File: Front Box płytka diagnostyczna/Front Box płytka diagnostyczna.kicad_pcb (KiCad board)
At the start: 2 copper layers, 54 x 27.7 mm, 7 parts, among them J1 hdmi wurth, J5 CAN

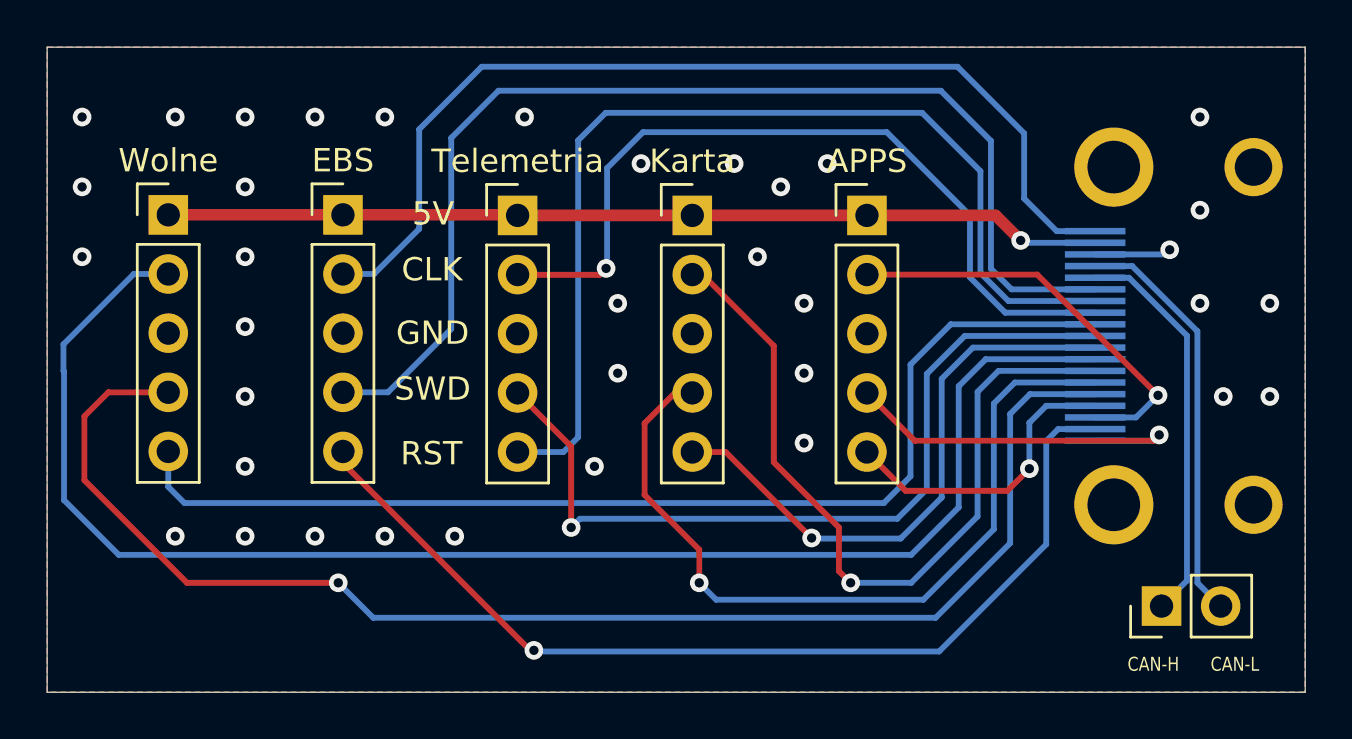
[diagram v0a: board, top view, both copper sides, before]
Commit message: PCB prepared for gerber generation
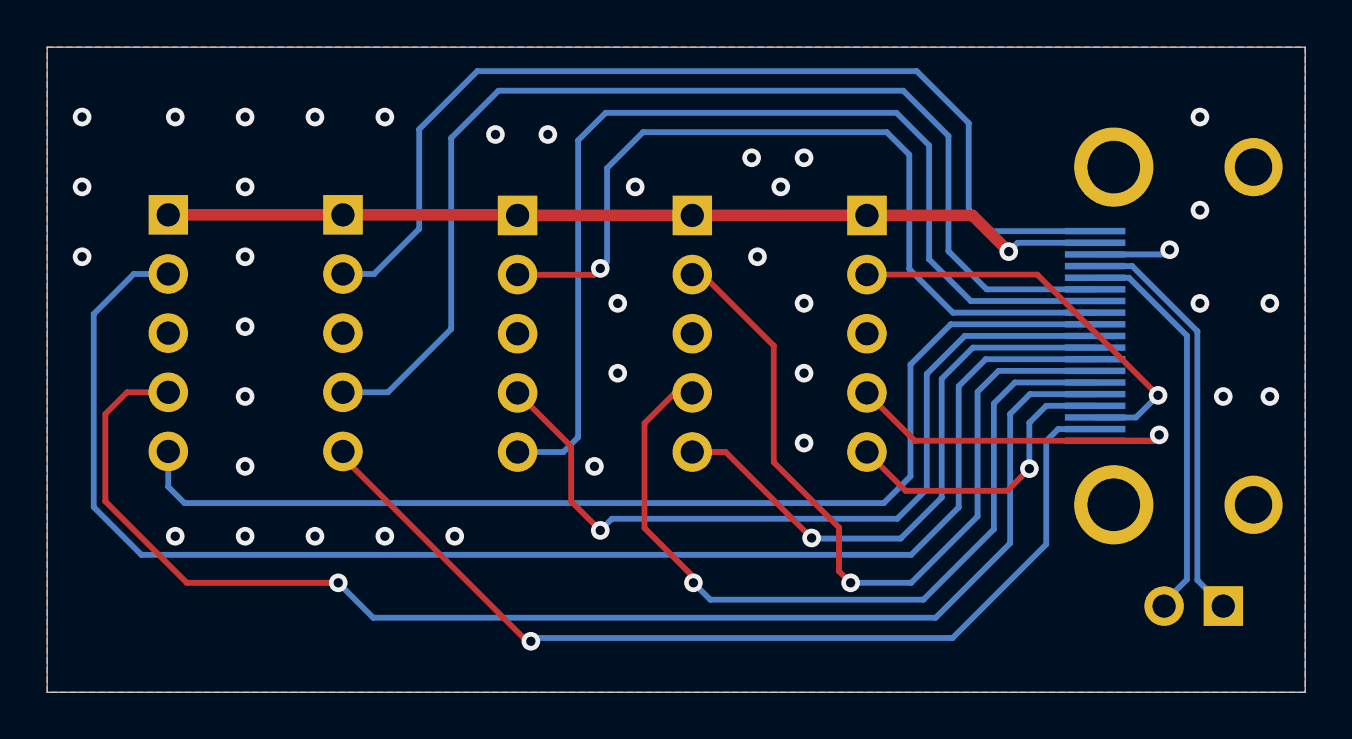
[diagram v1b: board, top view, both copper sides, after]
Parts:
- CAN1: renamed from J5; value CAN -> Male header 2.54mm; moved to B.Cu
- J1: renamed from APPS; value 5 -> APPS; moved to B.Cu
- J2: renamed from Karta; value 4 -> Karta; moved to B.Cu
- J3: renamed from Telemetria; value 3 -> Telemetria; moved to B.Cu
- J4: renamed from EBS; value 2 -> EBS; moved to B.Cu
- J5: renamed from Wolne; value 1 -> Wolne; moved to B.Cu
- moved CAN1 2.65 mm to (177.4, 110.7)
- turned J1 to 180 degrees
- turned J2 to 180 degrees
- turned J3 to 180 degrees
- turned J4 to 180 degrees
- turned J5 to 180 degrees
- renumbered J1 to HDMI1
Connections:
- CAN1 pad 1: /CAN-H -> /CAN-L
- CAN1 pad 2: /CAN-L -> /CAN-H
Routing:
- net /CLK5: track 64.2 -> 62.6 mm
- net /SWD5: track 59.8 -> 58.6 mm
- net /CLK3: track 34.6 -> 35.8 mm
- net /SWD3: track 35.5 -> 35.0 mm
- net /RST4: track 42.7 -> 42.2 mm
- net GND: vias 36 -> 37

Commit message: Even better silkscreen for diagnostic PCB
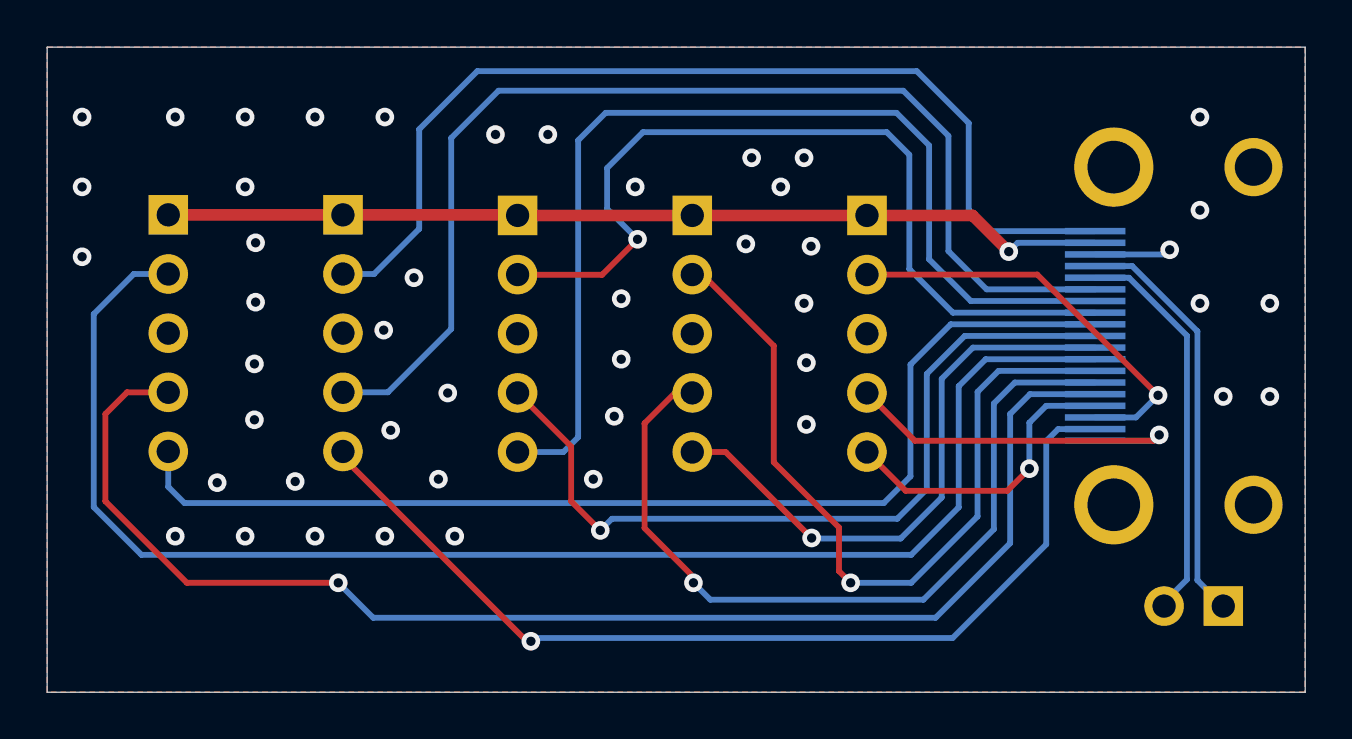
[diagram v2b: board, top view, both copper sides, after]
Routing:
- net /CLK3: track 35.8 -> 37.1 mm
- net GND: vias 37 -> 46
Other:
- board text added: "APPS"
- board text added: "EBS"
- board text added: "Karta"
- board text added: "Telemetria"
- board text added: "Wolne"

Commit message: quick revision
Added LED's to horizontal board, distance between sockets fix, Diagnostic Board 5v line delete and compatibility with HDMI fix
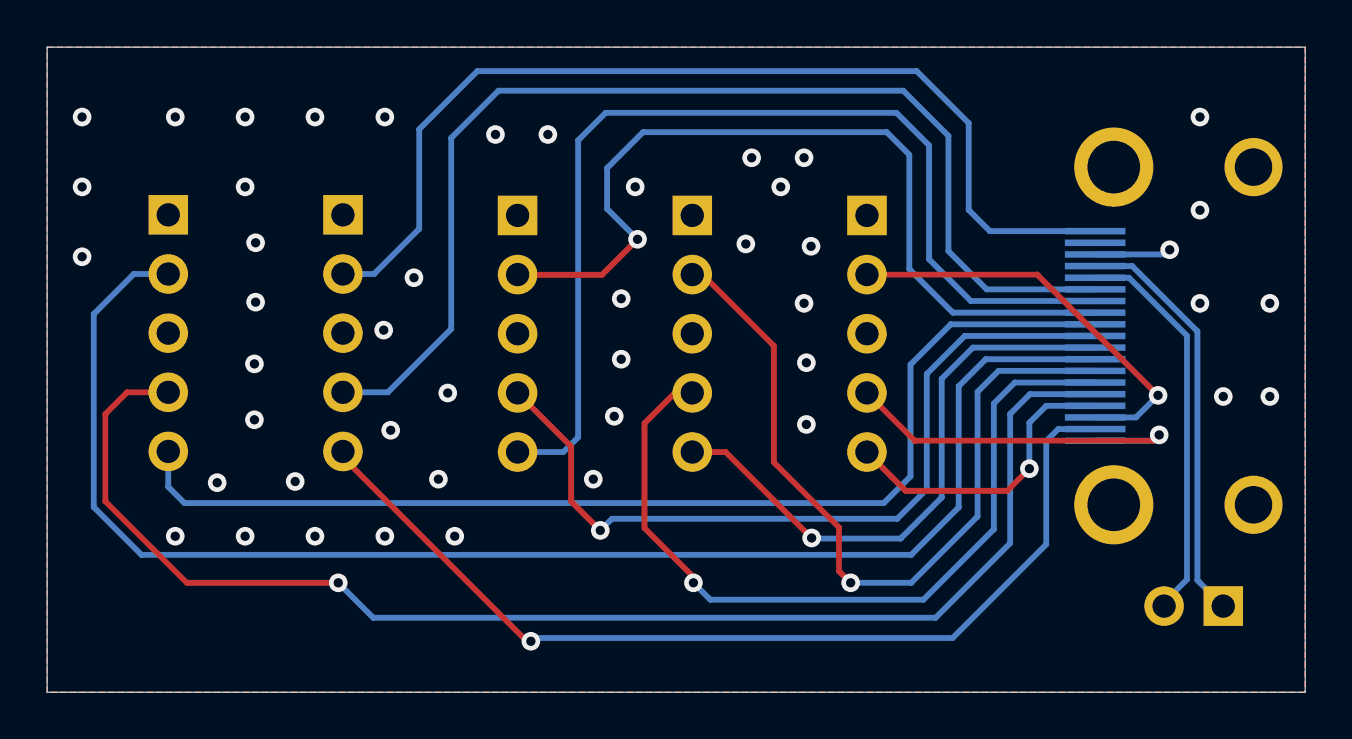
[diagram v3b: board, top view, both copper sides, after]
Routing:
- net +5V: track 40.6 -> 0.04 mm, vias 1 -> 0
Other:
- board text removed: "5V"
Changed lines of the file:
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@@
       (effects (font (size 1 1) (thickness 0.15)) (justify mirror))
     )
-    (fp_text value "APPS" (at 0 -12.49) (layer "B.SilkS")
+    (fp_text value "APPS" (at 30 -12.675) (layer "B.SilkS")
       (effects (font (size 1 1) (thickness 0.15)) (justify mirror))
     )
@@
       (effects (font (size 1 1) (thickness 0.15)) (justify mirror))
     )
-    (fp_text value "Wolne" (at 0 -12.49) (layer "B.SilkS")
+    (fp_text value "Wolne" (at -29.7 -12.7) (layer "B.SilkS")
       (effects (font (size 1 1) (thickness 0.15)) (justify mirror))
     )
@@
     (effects (font (size 1 1) (thickness 0.15)) (justify mirror))
   )
-  (gr_text "APPS" (at 162.1 91.2 180) (layer "B.SilkS")
-    (effects (font (size 1 1) (thickness 0.15)) (justify mirror))
-  )
-  (gr_text "5V" (at 158.4 93.925 180) (layer "B.SilkS")
+  (gr_text "APPS" (at 132.3 90.8 180) (layer "B.SilkS")
     (effects (font (size 1 1) (thickness 0.15)) (justify mirror))
   )
@@
     (effects (font (size 0.6 0.5) (thickness 0.1)) (justify mirror))
   )
-  (gr_text "Wolne" (at 132.16 91.25 180) (layer "B.SilkS")
+  (gr_text "Wolne" (at 161.9 91.3 180) (layer "B.SilkS")
     (effects (font (size 1 1) (thickness 0.15)) (justify mirror))
   )
   (gr_text "RST" (at 135.825 104.25) (layer "B.SilkS")
-    (effects (font (size 1 1) (thickness 0.15)) (justify mirror))
-  )
-  (gr_text "5V" (at 135.9 93.95) (layer "B.SilkS")
     (effects (font (size 1 1) (thickness 0.15)) (justify mirror))
   )
@@
   (segment (start 174.9 95.6) (end 175.1 95.4) (width 0.25) (layer "B.Cu") (net 1))
   (segment (start 171.9 95.6) (end 174.9 95.6) (width 0.25) (layer "B.Cu") (net 1))
-  (segment (start 139.6 93.9) (end 147.075 93.9) (width 0.5) (layer "F.Cu") (net 2))
-  (segment (start 168.19 95.48) (end 166.635 93.925) (width 0.5) (layer "F.Cu") (net 2))
-  (segment (start 154.6 93.925) (end 162.1 93.925) (width 0.5) (layer "F.Cu") (net 2))
-  (segment (start 147.1 93.925) (end 154.6 93.925) (width 0.5) (layer "F.Cu") (net 2))
   (segment (start 147.075 93.9) (end 147.1 93.925) (width 0.5) (layer "F.Cu") (net 2))
-  (segment (start 166.635 93.925) (end 162.1 93.925) (width 0.5) (layer "F.Cu") (net 2))
-  (segment (start 139.6 93.9) (end 132.1 93.9) (width 0.5) (layer "F.Cu") (net 2))
-  (via (at 168.19 95.48) (size 0.8) (drill 0.4) (layers "F.Cu" "B.Cu") (net 2))
-  (segment (start 168.57 95.1) (end 171.9 95.1) (width 0.25) (layer "B.Cu") (net 2))
-  (segment (start 168.19 95.48) (end 168.57 95.1) (width 0.25) (layer "B.Cu") (net 2))
   (segment (start 169.415 96.465) (end 162.1 96.465) (width 0.25) (layer "F.Cu") (net 3))
   (segment (start 174.6 101.65) (end 169.415 96.465) (width 0.25) (layer "F.Cu") (net 3))
